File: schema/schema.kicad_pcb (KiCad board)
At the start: 4 copper layers, 55.2 x 30.8 mm, 28 parts, among them M1 Motor, M2 Motor_Servo, Q1 2N7000, Q2 2N7000, Q3 2N7000, Q4 2N7000, SW1 SW_Push, U2 NRF24L01, U3 L9110H, U4 LM2937xT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

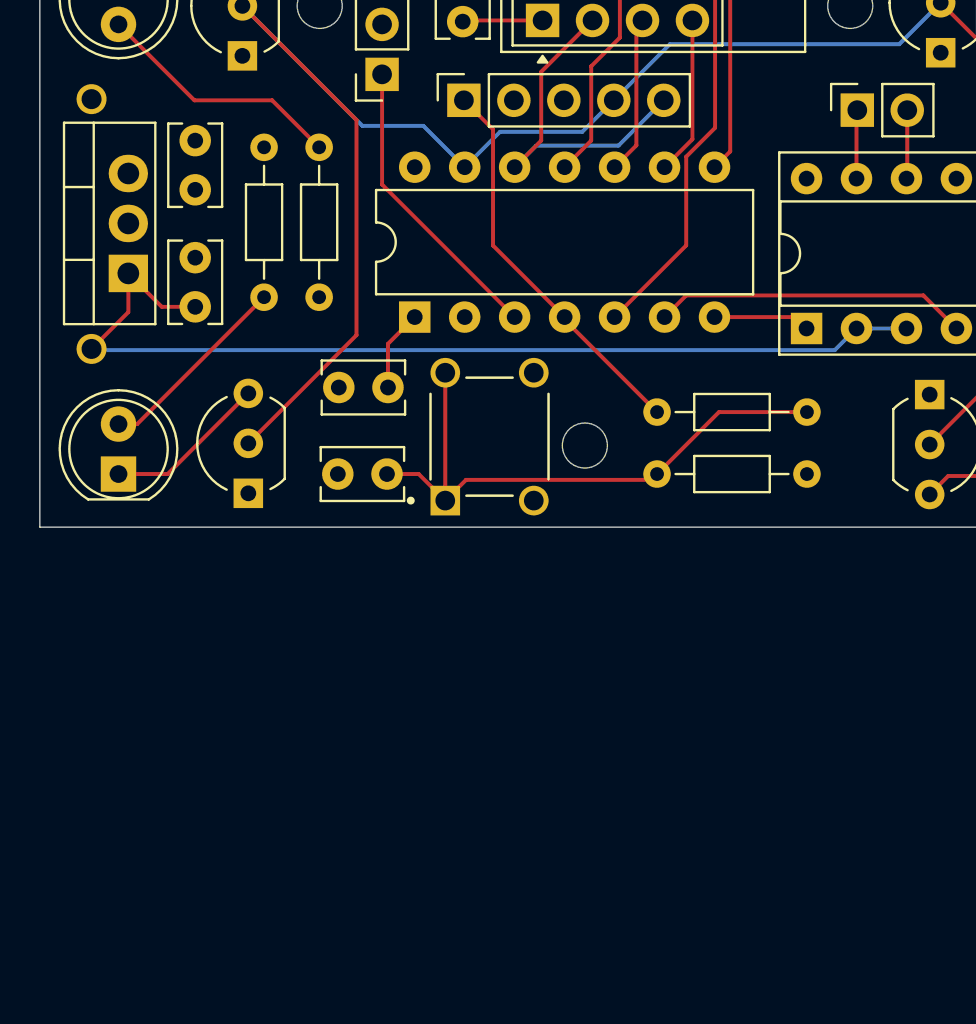
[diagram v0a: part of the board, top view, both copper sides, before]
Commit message: Add switch to schema
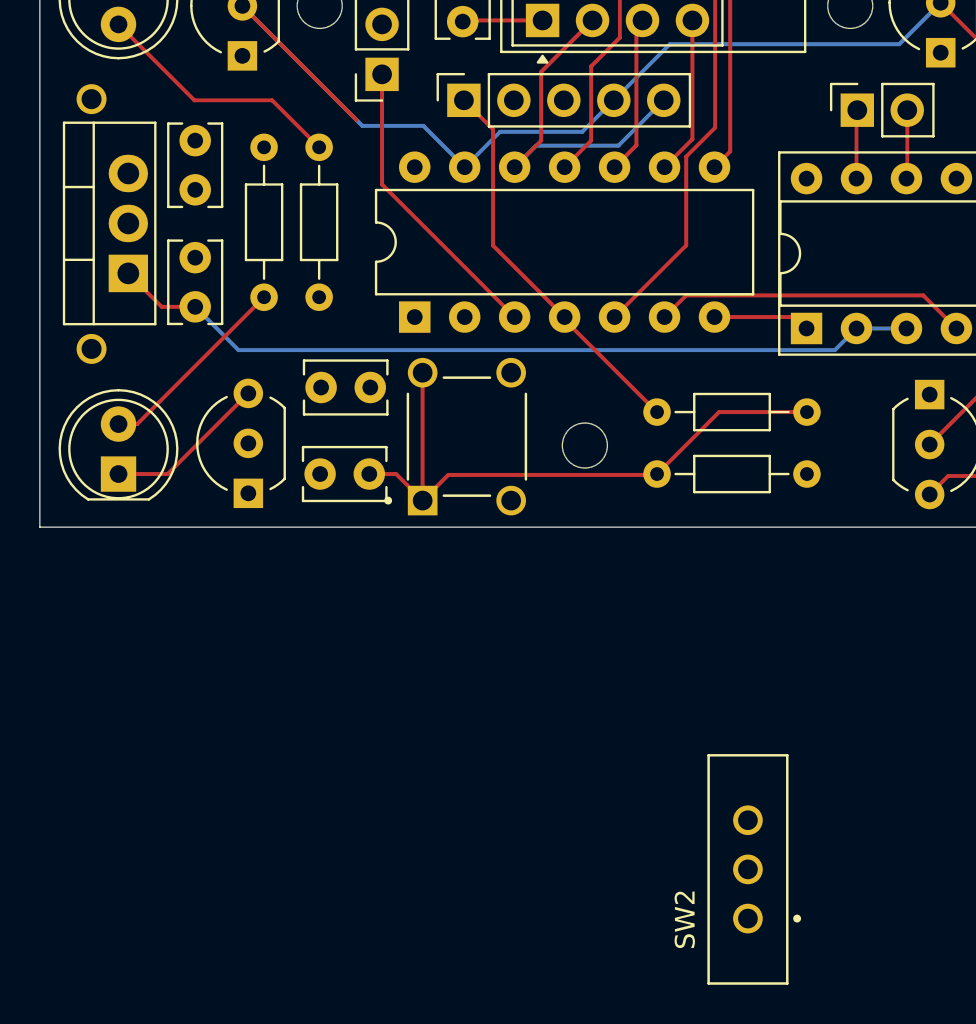
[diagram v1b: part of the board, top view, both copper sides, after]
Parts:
- added SW2: SW_SPDT, RC_Car_footprints:SW_EG1218, F.Cu at (78.5, 120.5)
- moved SW1 1.15 mm to (64.2, 98.5)
- moved C8 0.90 mm to (56.8, 96.0)
- moved C4 0.90 mm to (59.2, 100.4)
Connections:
- BT1 pad 1: +9V -> Net-(BT1-+)
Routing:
- net LIGHTS: track 93.5 -> 74.8 mm
- net +9V: track 50.6 -> 41.6 mm
- net MCU_SEL: track 8.24 -> 4.10 mm
- net Net-(C4-Pad1): track 30.3 -> 31.6 mm

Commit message: Refactors schematics
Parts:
- added D5: LED, LED_THT:LED_D5.0mm, F.Cu at (119.4, 85.5)
- added R7: 470, Resistor_THT:R_Axial_DIN0204_L3.6mm_D1.6mm_P7.62mm_Horizontal, F.Cu at (92.2, 92.9)
- moved SW2 49.7 mm to (41.0, 87.8)
- moved M2 7.55 mm to (52.4, 80.0)
- moved D3 5.50 mm to (99.2, 75.0)
- moved D4 5.50 mm to (99.3, 100.5)
- moved Q3 5.50 mm to (93.8, 79.0)
- moved Q4 5.50 mm to (93.2, 96.4)
- moved D1 4.50 mm to (42.0, 75.0)
- moved D2 4.50 mm to (42.0, 100.4)
- moved Q1 4.50 mm to (48.3, 79.1)
- moved Q2 4.50 mm to (48.6, 101.4)
- moved C4 4.05 mm to (55.2, 100.4)
- moved C8 4.05 mm to (52.8, 96.0)
- moved R5 3.00 mm to (95.3, 92.9)
- moved R6 3.00 mm to (98.5, 85.3)
- moved SW1 2.51 mm to (61.7, 98.5), turned to 180 degrees
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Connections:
- BT1 pad 2: GND -> MCU_SEL
- C4 pad 2: GND -> MCU_SEL
- C5 pad 1: MCU_SEL -> +3.3V
- C5 pad 2: GND -> MCU_SEL
- C6 pad 2: GND -> MCU_SEL
- C7 pad 1: MCU_SEL -> +3.3V
- C7 pad 2: GND -> MCU_SEL
- C8 pad 1: GND -> MCU_SEL
- C8 pad 2: MCU_SEL -> +3.3V
- M2 pad 1: PWM_TEMP -> PWM6
- M2 pad 2: MCU_SEL -> +3.3V
- M2 pad 3: GND -> MCU_SEL
- PRG1 pad 2: MCU_SEL -> +3.3V
- PRG1 pad 3: GND -> MCU_SEL
- Q1 pad 1: GND -> MCU_SEL
- Q2 pad 1: GND -> MCU_SEL
- Q3 pad 1: GND -> MCU_SEL
- Q4 pad 1: GND -> MCU_SEL
- R1 pad 1: MCU_SEL -> +3.3V
- R3 pad 2: MCU_SEL -> +3.3V
- R4 pad 1: MCU_SEL -> +3.3V
- R5 pad 1: MCU_SEL -> +3.3V
- R6 pad 1: MCU_SEL -> +3.3V
- SW1 pad 3: GND -> MCU_SEL
- SW1 pad 4: GND -> MCU_SEL
- U2 pad 1: GND -> MCU_SEL
- U2 pad 2: MCU_SEL -> +3.3V
- U3 pad 4: PWM6 -> PWM5.1
- U3 pad 5: GND -> MCU_SEL
- U3 pad 8: GND -> MCU_SEL
- U4 pad 2: GND -> MCU_SEL
- U4 pad 3: MCU_SEL -> +3.3V
- U5 pad 1: MCU_SEL -> +3.3V
- U5 pad 11: MOSI -> PWM6
- U5 pad 14: GND -> MCU_SEL
- U5 pad 3: PWM_TEMP -> MOSI
- U5 pad 6: PWM6 -> PWM5.1
- U5 pad 7: PWM5 -> ~{CSN}
- U5 pad 8: ~{CSN} -> PWM5
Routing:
- net LIGHTS: track 74.8 -> 0.00 mm
- net +9V: track 41.6 -> 0.00 mm
- net Net-(C4-Pad1): track 31.6 -> 0.00 mm
- net IRQ: track 20.2 -> 0.00 mm
- net RESET: track 19.9 -> 0.00 mm
- net ~{CSN}: track 18.2 -> 0.00 mm
- net CE: track 18.1 -> 0.00 mm
- net PWM6: track 16.0 -> 0.00 mm
- net PWM_TEMP: track 15.1 -> 0.00 mm
- net Net-(D1-A): track 12.8 -> 0.00 mm
- net MOSI: track 11.6 -> 0.00 mm
- net Net-(D2-A): track 10.1 -> 0.00 mm
- net SCLK: track 8.39 -> 0.00 mm
- net Net-(D3-A): track 8.31 -> 0.00 mm
- net Net-(D2-K): track 8.30 -> 0.00 mm
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- added copper zone on In1.Cu, net MCU_SEL
- removed copper zone on In1.Cu, net GND
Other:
- board size 55.2 x 30.8 mm -> 64.6 x 30.8 mm
